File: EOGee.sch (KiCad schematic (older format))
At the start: 48 parts, among them J101 USB_B_Micro, J102 AudioJack3, SW101 SW_Push_45deg, SW102 SW_Push_45deg, U101 LMV324, U102 AD8226ARMZ, U103 AP2210, U105 STM32F042F4Px

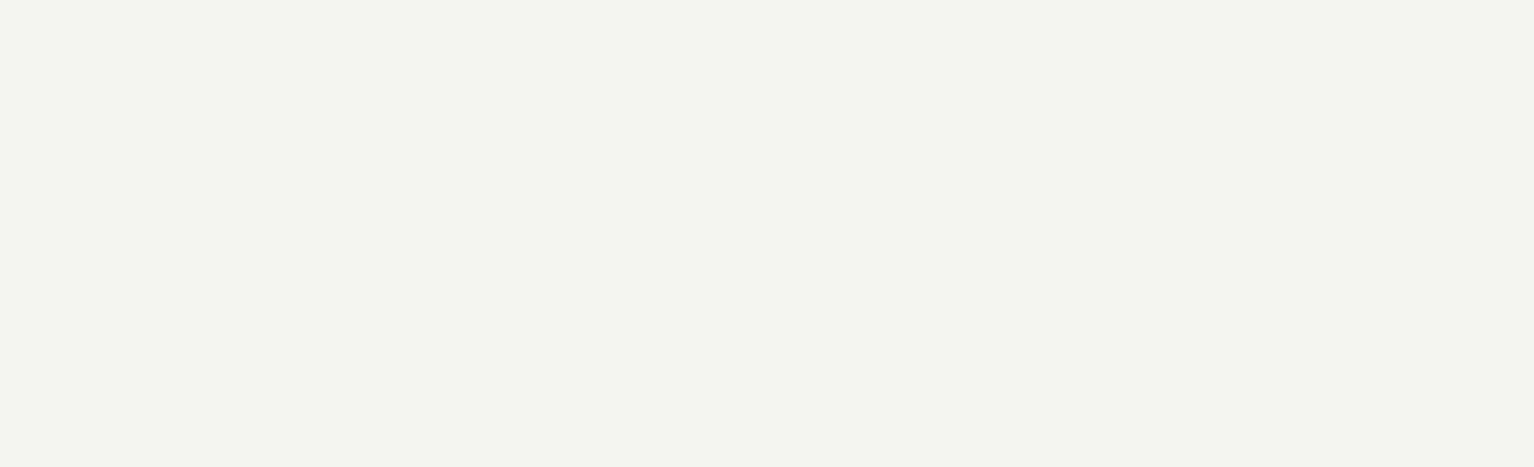
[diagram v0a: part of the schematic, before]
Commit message: add name to schematic:
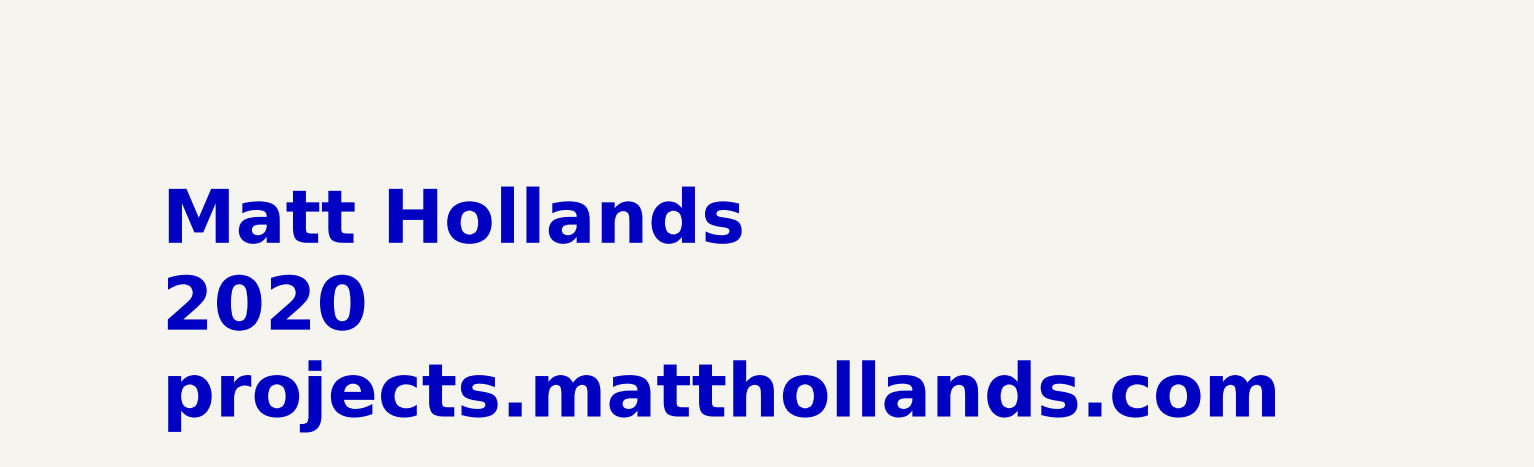
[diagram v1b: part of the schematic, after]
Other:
- note added: "Matt Hollands\n2020\nprojects.matthollands.com"
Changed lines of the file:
@@
 Wire Wire Line
 	7000 8900 7000 9000
+Text Notes 11250 9800 0    236  ~ 47
+Matt Hollands\n2020\nprojects.matthollands.com
 $EndSCHEMATC
